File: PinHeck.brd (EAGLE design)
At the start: 359.2 x 152.3 mm, 337 parts, among them IC1 FT232RL-REEL, IC2 PIC32MX795F512L-80I/PT, IC3 CD74HCT244E, IC4 CD74HCT244E, IC5 ULN2803A, J1 500075-1517, J11 No Load, J2 500075-1517, J3 N/A, J6 161-3507-E, P1 TC33X-2-103E, SW1 101-0134-EV, SW2 101-0134-EV, U1 P8X32A-Q44, U10 74HCT2G04GV,125, U11 74HC165D,652, U12 74HC165D,652, U14 MC74HC08ADG, U15 MC74HC08ADG, U16 MC74HC08ADG, U17 MC74HC08ADG, U18 MC74HC08ADG, U19 MC74HC08ADG, U2 FT230XS-R, U20 TIP107, U21 TIP107, U22 TIP107, U23 TIP107, U24 TIP107, U25 TIP107, U26 TIP107, U27 TIP107, U28 TIP102, U29 TIP102, U3 74HC595D-Q100, U30 TIP102, U31 TIP102, U32 TIP102, U33 TIP102, U34 TIP102, U35 TIP102, U36 WS2801, U37 TIP102, U38 WS2801, U39 LM2937IMP-3.3/NOPB, U4 24LC1025-I/P, U40 TIP102, U41 TIP102, U42 TIP102, U43 TIP102, U44 TIP102, U45 TIP102, U46 TIP102, U47 TIP102, U48 TIP102, U49 TIP102, U5 74HC595D-Q100, U50 TIP102, U51 TIP102, U52 CD74HC123M96, U6 TIP102, U7 TIP102, U8 TIP102, U9 TIP102, X1 FQ7050B-8.000, X2 ECS-65-20-4X

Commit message: Added Bluetooth
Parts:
- added BT1: RN-41, PP_Sensors:RN-41
- added BT_RX, BT_TX, USBDM, USBDP, VBUS: (no value), PP_Connectors:HEADER_01X02_PTH
- added C28: .1uF, PP_Passives:0805
- added C29: 10uF, PP_Passives:1206
- added R137, R138, R139: 10K, PP_Passives:0805
- added SW3: 101-0134-EV, PP_Electromechanical:101-0134-EV
- added SW4: 0S102011MS2QS1, PP_Electromechanical:0S102011MS2QS1
- moved LOGO1 19.3 mm to (30.5, 105.7)
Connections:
- new net BT_RESET: BT1.5, R138.2, SW4.1
- new net BT_RX: BT1.13, BT_RX.1
- new net BT_TX: BT1.14, BT_TX.1
- new net FT232_RESET: IC1.19, R139.1, SW4.3
- net 3.3V: now also BT1.11, C28.2, C29.1, R137.2, SW4.2
- net DM: now also USBDM.2
- net DP: now also USBDP.2
- net FT_3.3V: no longer IC1.19
- net GND: now also BT1.1, BT1.12, BT1.25, BT1.27, BT1.28, BT1.29, C28.1, C29.2, R138.1, R139.2, SW3.2
- net RG9: now also R137.1, SW3.1
- net RX_PIC32: now also BT_RX.2
- net TX_PIC32: now also BT_TX.2
- net USBD+: now also USBDP.1
- net USBD-: now also USBDM.1
- net USB_BUS: now also VBUS.2
- net VUSB: now also VBUS.1
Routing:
- net BT_RESET: track 0.00 -> 119.0 mm, vias 0 -> 2
- net TX_PIC32: track 49.6 -> 137.7 mm, vias 2 -> 6
- net RX_PIC32: track 39.8 -> 124.8 mm, vias 2 -> 6
- net USBD+: track 0.00 -> 72.6 mm
- net USBD-: track 0.00 -> 66.5 mm
- net VUSB: track 0.00 -> 59.3 mm
- net 3.3V: track 1201.2 -> 1254.0 mm, vias 31 -> 34
- net RG9: track 0.00 -> 44.0 mm, vias 0 -> 2
- net FT232_RESET: track 0.00 -> 30.9 mm
- net USB_BUS: track 27.0 -> 42.0 mm
- net DM: track 7.45 -> 20.6 mm
- net BT_RX: track 0.00 -> 11.0 mm
- net BT_TX: track 0.00 -> 9.65 mm
- net DP: track 9.01 -> 17.6 mm
- net FT_3.3V: track 47.9 -> 45.3 mm
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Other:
- board text added: "BT"
- board text added: "USB"

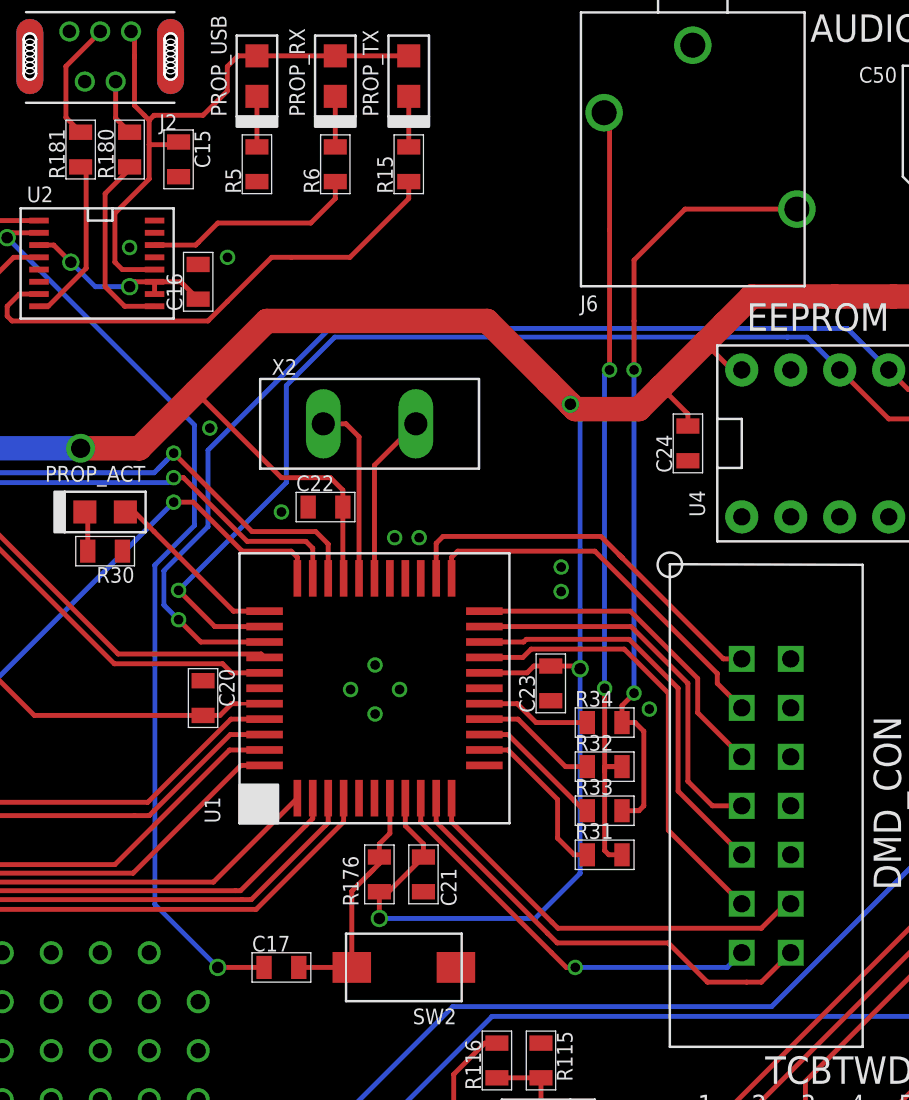
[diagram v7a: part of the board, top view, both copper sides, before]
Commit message: Added 2 more audio channels
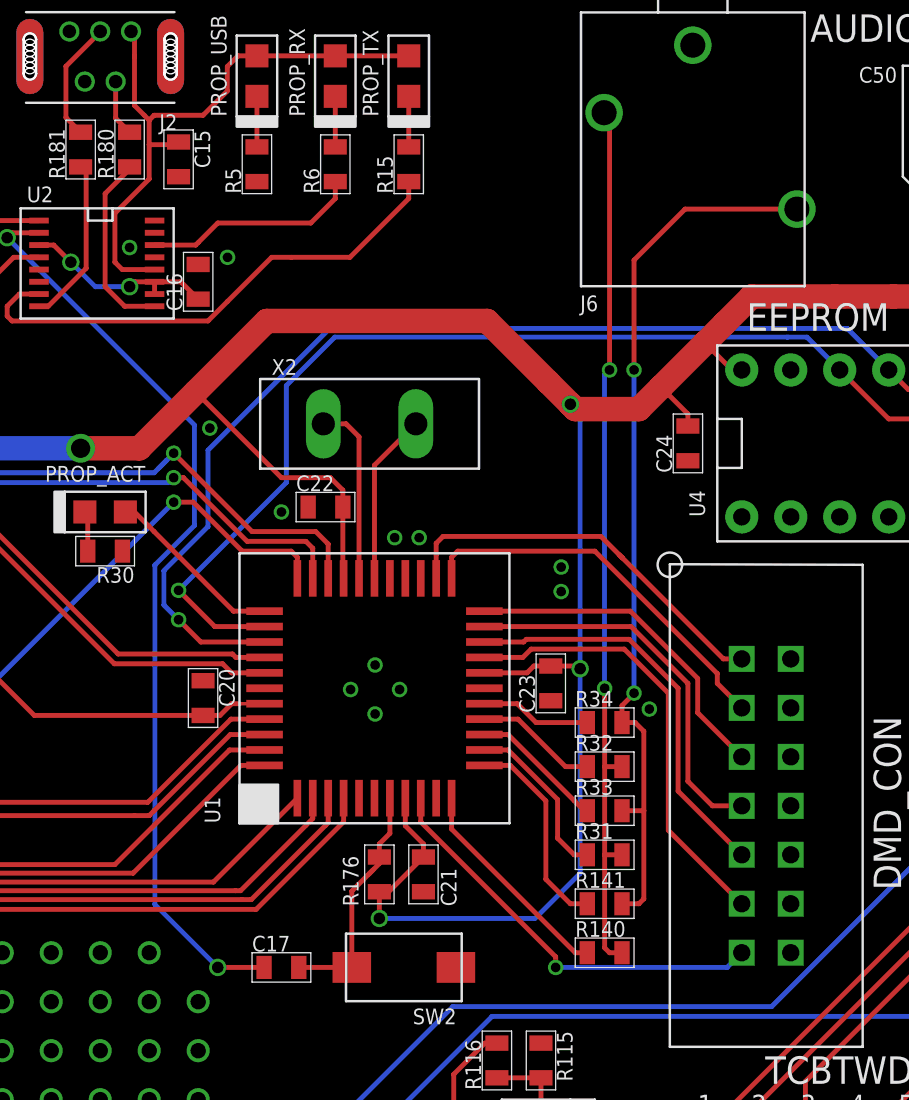
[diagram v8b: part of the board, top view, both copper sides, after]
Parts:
- added R140, R141: 4.7K, PP_Passives:0805
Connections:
- net GND: now also DMD_CON.8, DMD_CON.9
- net P10: now also R140.1; no longer DMD_CON.9
- net P11: now also R141.1
- net P9: no longer DMD_CON.8
- net S_L: now also R140.2
- net S_R: now also R141.2
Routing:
- net P9: track 23.7 -> 0.00 mm
- net P11: track 0.00 -> 10.7 mm
- net P10: track 21.6 -> 11.3 mm
- net S_R: track 40.2 -> 46.2 mm
- net S_L: track 41.3 -> 46.3 mm
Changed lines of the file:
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@@
 <attribute name="NAME" x="48.768" y="154.7495" size="0.8128" layer="25" font="vector"/>
 </element>
+<element name="R140" library="PP_Passives" package="0805" value="4.7K" x="287.782" y="124.46"/>
+<element name="R141" library="PP_Passives" package="0805" value="4.7K" x="287.782" y="127"/>
 </elements>
 <signals>
@@
 <contactref element="R138" pad="1"/>
 <contactref element="R139" pad="2"/>
+<contactref element="DMD_CON" pad="9"/>
+<contactref element="DMD_CON" pad="8"/>
 </signal>
 <signal name="N$4">
@@
 <signal name="P11">
 <contactref element="U1" pad="12"/>
+<contactref element="R141" pad="1"/>
+<wire x1="281.544" y1="134.176" x2="282.892" y2="134.176" width="0.254" layer="1"/>
+<wire x1="282.892" y1="134.176" x2="284.734" y2="132.334" width="0.254" layer="1"/>
+<wire x1="284.734" y1="132.334" x2="284.734" y2="128.27" width="0.254" layer="1"/>
+<wire x1="284.734" y1="128.27" x2="286.004" y2="127" width="0.254" layer="1"/>
+<wire x1="286.004" y1="127" x2="286.882" y2="127" width="0.254" layer="1"/>
 </signal>
 <signal name="P10">
 <contactref element="U1" pad="11"/>
-<contactref element="DMD_CON" pad="9"/>
-<wire x1="279.844" y1="132.476" x2="279.844" y2="131.2465" width="0.254" layer="1"/>
-<wire x1="279.844" y1="131.2465" x2="285.045" y2="126.0455" width="0.254" layer="1"/>
-<wire x1="285.045" y1="126.0455" x2="285.3605" y2="125.73" width="0.254" layer="1"/>
-<wire x1="285.3605" y1="125.73" x2="295.91" y2="125.73" width="0.254" layer="1"/>
-<wire x1="295.91" y1="125.73" x2="297.18" y2="127" width="0.254" layer="1"/>
-<wire x1="297.18" y1="127" x2="297.434" y2="127" width="0.254" layer="1"/>
+<contactref element="R140" pad="1"/>
+<wire x1="279.844" y1="132.476" x2="279.844" y2="130.874" width="0.254" layer="1"/>
+<wire x1="279.844" y1="130.874" x2="286.258" y2="124.46" width="0.254" layer="1"/>
+<wire x1="286.258" y1="124.46" x2="286.882" y2="124.46" width="0.254" layer="1"/>
 </signal>
 <signal name="P9">
 <contactref element="U1" pad="10"/>
-<contactref element="DMD_CON" pad="8"/>
-<wire x1="279.044" y1="132.476" x2="279.044" y2="131.2465" width="0.254" layer="1"/>
-<wire x1="279.044" y1="131.2465" x2="284.8145" y2="125.476" width="0.254" layer="1"/>
-<wire x1="284.8145" y1="125.476" x2="285.3225" y2="124.968" width="0.254" layer="1"/>
-<wire x1="285.3225" y1="124.968" x2="291.084" y2="124.968" width="0.254" layer="1"/>
-<wire x1="291.084" y1="124.968" x2="293.116" y2="122.936" width="0.254" layer="1"/>
-<wire x1="293.116" y1="122.936" x2="295.148" y2="122.936" width="0.254" layer="1"/>
-<wire x1="295.148" y1="122.936" x2="295.91" y2="122.936" width="0.254" layer="1"/>
-<wire x1="295.91" y1="122.936" x2="297.434" y2="124.46" width="0.254" layer="1"/>
 </signal>
 <signal name="P8">
@@
 <contactref element="DMD_CON" pad="7"/>
 <wire x1="278.244" y1="132.476" x2="278.244" y2="131.2465" width="0.254" layer="1"/>
-<wire x1="278.244" y1="131.2465" x2="285.0305" y2="124.46" width="0.254" layer="1"/>
-<wire x1="285.0305" y1="124.46" x2="285.7925" y2="123.698" width="0.254" layer="1"/>
-<wire x1="285.7925" y1="123.698" x2="286.258" y2="123.698" width="0.254" layer="1"/>
-<via x="286.258" y="123.698" extent="1-16" drill="0.5"/>
-<wire x1="286.258" y1="123.698" x2="294.132" y2="123.698" width="0.254" layer="16"/>
+<via x="285.242" y="123.698" extent="1-16" drill="0.5"/>
+<wire x1="285.242" y1="123.698" x2="294.132" y2="123.698" width="0.254" layer="16"/>
 <wire x1="294.132" y1="123.698" x2="294.894" y2="124.46" width="0.254" layer="16"/>
+<wire x1="278.244" y1="131.2465" x2="285.242" y2="124.2485" width="0.254" layer="1"/>
+<wire x1="285.242" y1="124.2485" x2="285.242" y2="123.698" width="0.254" layer="1"/>
 </signal>
 <signal name="X0">
@@
 <wire x1="255.524" y1="158.921565625" x2="255.524" y2="146.979290625" width="0.254" layer="1"/>
 <wire x1="255.524" y1="146.979290625" x2="262.549290625" y2="139.954" width="0.254" layer="1"/>
-<wire x1="262.549290625" y1="139.954" x2="269.966" y2="139.954" width="0.254" layer="1"/>
-<wire x1="269.966" y1="139.954" x2="270.144" y2="139.776" width="0.254" layer="1"/>
+<wire x1="262.549290625" y1="139.954" x2="268.478" y2="139.954" width="0.254" layer="1"/>
+<wire x1="268.478" y1="139.954" x2="268.656" y2="139.776" width="0.254" layer="1"/>
+<wire x1="268.656" y1="139.776" x2="270.144" y2="139.776" width="0.254" layer="1"/>
 </signal>
 <signal name="N$10">
@@
 <wire x1="287.7747" y1="154.4247" x2="287.7747" y2="138.1833" width="0.254" layer="16"/>
 <wire x1="287.7747" y1="138.1833" x2="287.782" y2="138.176" width="0.254" layer="16"/>
-<wire x1="288.682" y1="134.112" x2="288.0025" y2="134.112" width="0.254" layer="1"/>
-<wire x1="288.682" y1="129.54" x2="288.0025" y2="129.54" width="0.254" layer="1"/>
-<wire x1="288.682" y1="134.112" x2="288.0025" y2="134.112" width="0.254" layer="1"/>
+<wire x1="288.682" y1="134.112" x2="287.782" y2="134.112" width="0.254" layer="1"/>
 <via x="288.036" y="154.686" extent="1-16" drill="0.5" diameter="0.8048"/>
 <via x="287.782" y="138.176" extent="1-16" drill="0.5" diameter="0.8048"/>
-<wire x1="288.0025" y1="129.54" x2="287.782" y2="129.7605" width="0.254" layer="1"/>
-<wire x1="287.782" y1="129.7605" x2="287.782" y2="133.858" width="0.254" layer="1"/>
-<wire x1="287.782" y1="133.858" x2="287.782" y2="138.176" width="0.254" layer="1"/>
-<wire x1="288.0025" y1="134.112" x2="287.782" y2="134.112" width="0.254" layer="1"/>
-<wire x1="287.782" y1="134.112" x2="287.782" y2="133.858" width="0.254" layer="1"/>
-<wire x1="288.036" y1="154.686" x2="288.036" y2="161.946" width="0.254" layer="1"/>
+<wire x1="287.782" y1="134.112" x2="287.782" y2="138.176" width="0.254" layer="1"/>
+<wire x1="288.036" y1="154.686" x2="288.036" y2="167.746" width="0.254" layer="1"/>
 <contactref element="J6" pad="5"/>
-<wire x1="288.036" y1="161.946" x2="288.036" y2="167.746" width="0.254" layer="1"/>
 <wire x1="288.036" y1="167.746" x2="287.754" y2="168.028" width="0.254" layer="1"/>
+<contactref element="R140" pad="2"/>
+<wire x1="288.682" y1="124.46" x2="288.036" y2="124.46" width="0.254" layer="1"/>
+<wire x1="288.036" y1="124.46" x2="287.782" y2="124.714" width="0.254" layer="1"/>
+<wire x1="287.782" y1="124.714" x2="287.782" y2="129.54" width="0.254" layer="1"/>
+<wire x1="287.782" y1="129.54" x2="287.782" y2="134.112" width="0.254" layer="1"/>
+<wire x1="288.682" y1="129.54" x2="287.782" y2="129.54" width="0.254" layer="1"/>
 </signal>
 <signal name="S_R">
@@
 <contactref element="R34" pad="2"/>
 <wire x1="288.682" y1="136.398" x2="289.3615" y2="136.398" width="0.254" layer="1"/>
-<wire x1="288.682" y1="131.826" x2="289.3615" y2="131.826" width="0.254" layer="1"/>
 <wire x1="288.682" y1="136.398" x2="288.682" y2="137.2775" width="0.254" layer="1"/>
 <via x="289.306" y="154.686" extent="1-16" drill="0.5" diameter="0.8048"/>
@@
 <wire x1="288.682" y1="137.2775" x2="289.306" y2="137.9015" width="0.254" layer="1"/>
 <wire x1="289.306" y1="137.9015" x2="289.306" y2="137.922" width="0.254" layer="1"/>
-<wire x1="289.3615" y1="131.826" x2="289.56" y2="131.826" width="0.254" layer="1"/>
-<wire x1="289.56" y1="131.826" x2="289.814" y2="132.08" width="0.254" layer="1"/>
-<wire x1="289.814" y1="132.08" x2="289.814" y2="135.9455" width="0.254" layer="1"/>
 <wire x1="289.814" y1="135.9455" x2="289.3615" y2="136.398" width="0.254" layer="1"/>
-<wire x1="289.306" y1="154.686" x2="289.306" y2="157.226" width="0.254" layer="1"/>
-<wire x1="289.306" y1="157.226" x2="289.306" y2="160.38" width="0.254" layer="1"/>
+<wire x1="289.306" y1="154.686" x2="289.306" y2="160.38" width="0.254" layer="1"/>
 <contactref element="J6" pad="2"/>
 <wire x1="289.306" y1="160.38" x2="291.954" y2="163.028" width="0.254" layer="1"/>
 <wire x1="291.954" y1="163.028" x2="297.754" y2="163.028" width="0.254" layer="1"/>
+<contactref element="R141" pad="2"/>
+<wire x1="288.682" y1="127" x2="289.56" y2="127" width="0.254" layer="1"/>
+<wire x1="289.56" y1="127" x2="289.814" y2="127.254" width="0.254" layer="1"/>
+<wire x1="289.814" y1="127.254" x2="289.814" y2="131.826" width="0.254" layer="1"/>
+<wire x1="289.814" y1="131.826" x2="289.814" y2="135.9455" width="0.254" layer="1"/>
+<wire x1="288.682" y1="131.826" x2="289.814" y2="131.826" width="0.254" layer="1"/>
 </signal>
 <signal name="5V">
